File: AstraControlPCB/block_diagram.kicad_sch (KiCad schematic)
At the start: 0 parts

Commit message: Update wks file
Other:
- sheet 5V Protection: file 5V_Protection.kicad_sch -> 5v_protection.kicad_sch
- company: (none) -> LiveAstra Technologies
- title: Block Diagram -> AstraControl - Root
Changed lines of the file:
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@@
 	(paper "A4")
 	(title_block
-		(title "Block Diagram")
+		(title "AstraControl - Root")
+		(date "2024-08-26")
+		(rev "A")
+		(company "LiveAstra Technologies")
 	)
 	(junction
@@
 		(effects
 			(font
+				(face "ING Me")
 				(size 1.27 1.27)
 			)
@@
 		(effects
 			(font
+				(face "ING Me")
 				(size 1.27 1.27)
 			)
@@
 		(effects
 			(font
+				(face "ING Me")
 				(size 1.27 1.27)
 			)
@@
 		(effects
 			(font
+				(face "ING Me")
 				(size 1.27 1.27)
 			)
@@
 		(effects
 			(font
+				(face "ING Me")
 				(size 1.27 1.27)
 			)
@@
 		(effects
 			(font
+				(face "ING Me")
 				(size 1.27 1.27)
 			)
@@
 		(effects
 			(font
+				(face "ING Me")
 				(size 1.27 1.27)
 			)
@@
 		(effects
 			(font
+				(face "ING Me")
 				(size 1.27 1.27)
 			)
@@
 		(effects
 			(font
+				(face "ING Me")
 				(size 1.27 1.27)
 			)
@@
 		(effects
 			(font
+				(face "ING Me")
 				(size 1.27 1.27)
 			)
@@
 			)
 		)
-		(property "Sheetfile" "5V_Protection.kicad_sch"
+		(property "Sheetfile" "5v_protection.kicad_sch"
 			(at 50.8 33.6046 0)
 			(effects

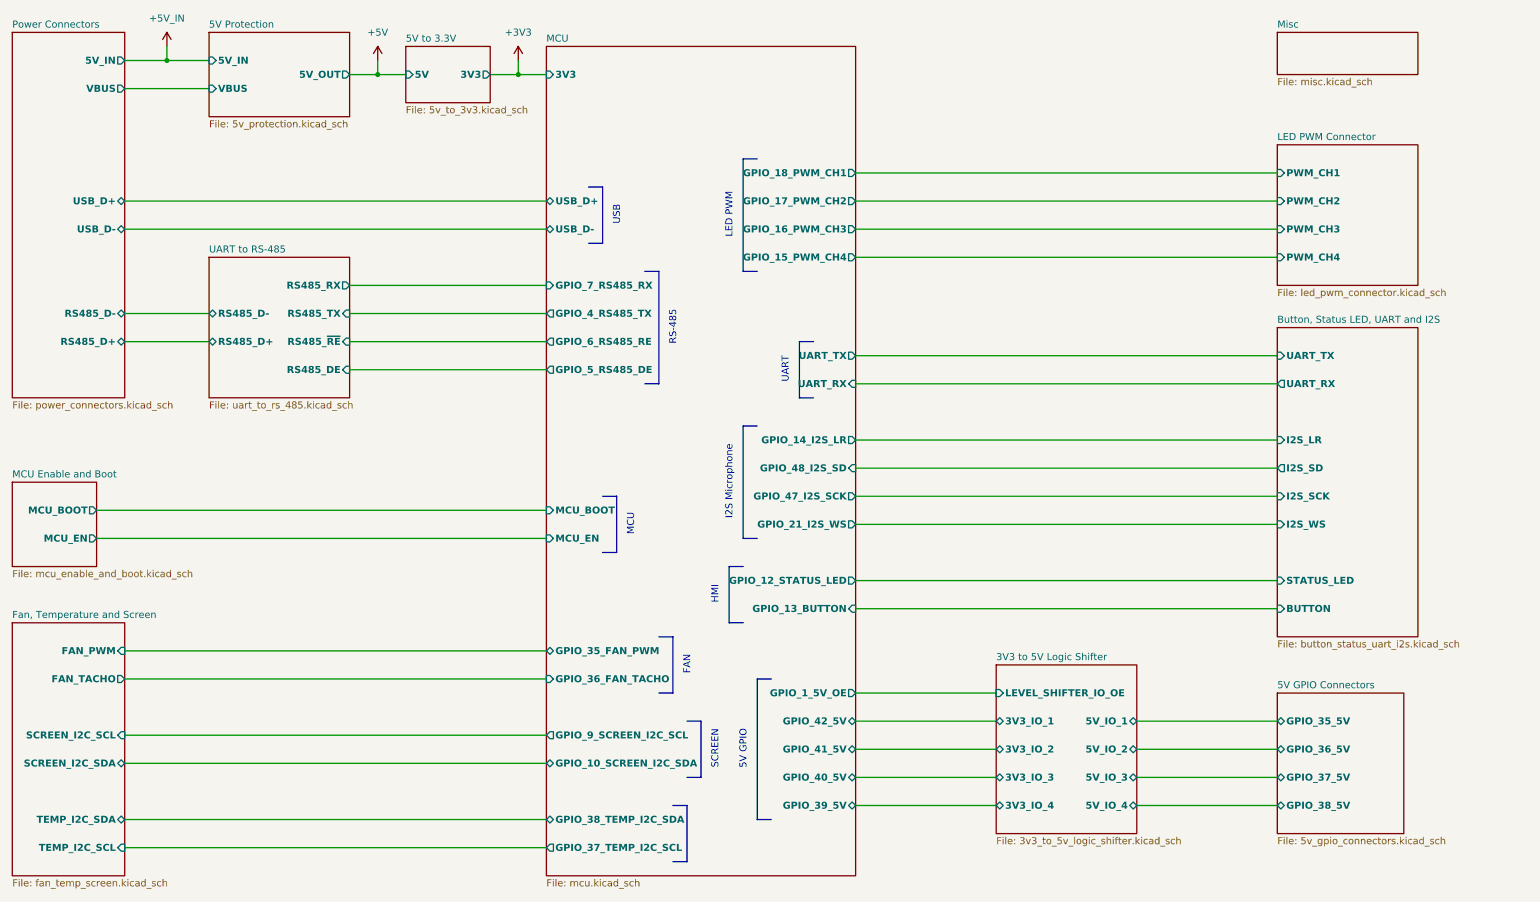
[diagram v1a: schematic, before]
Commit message: move template to root
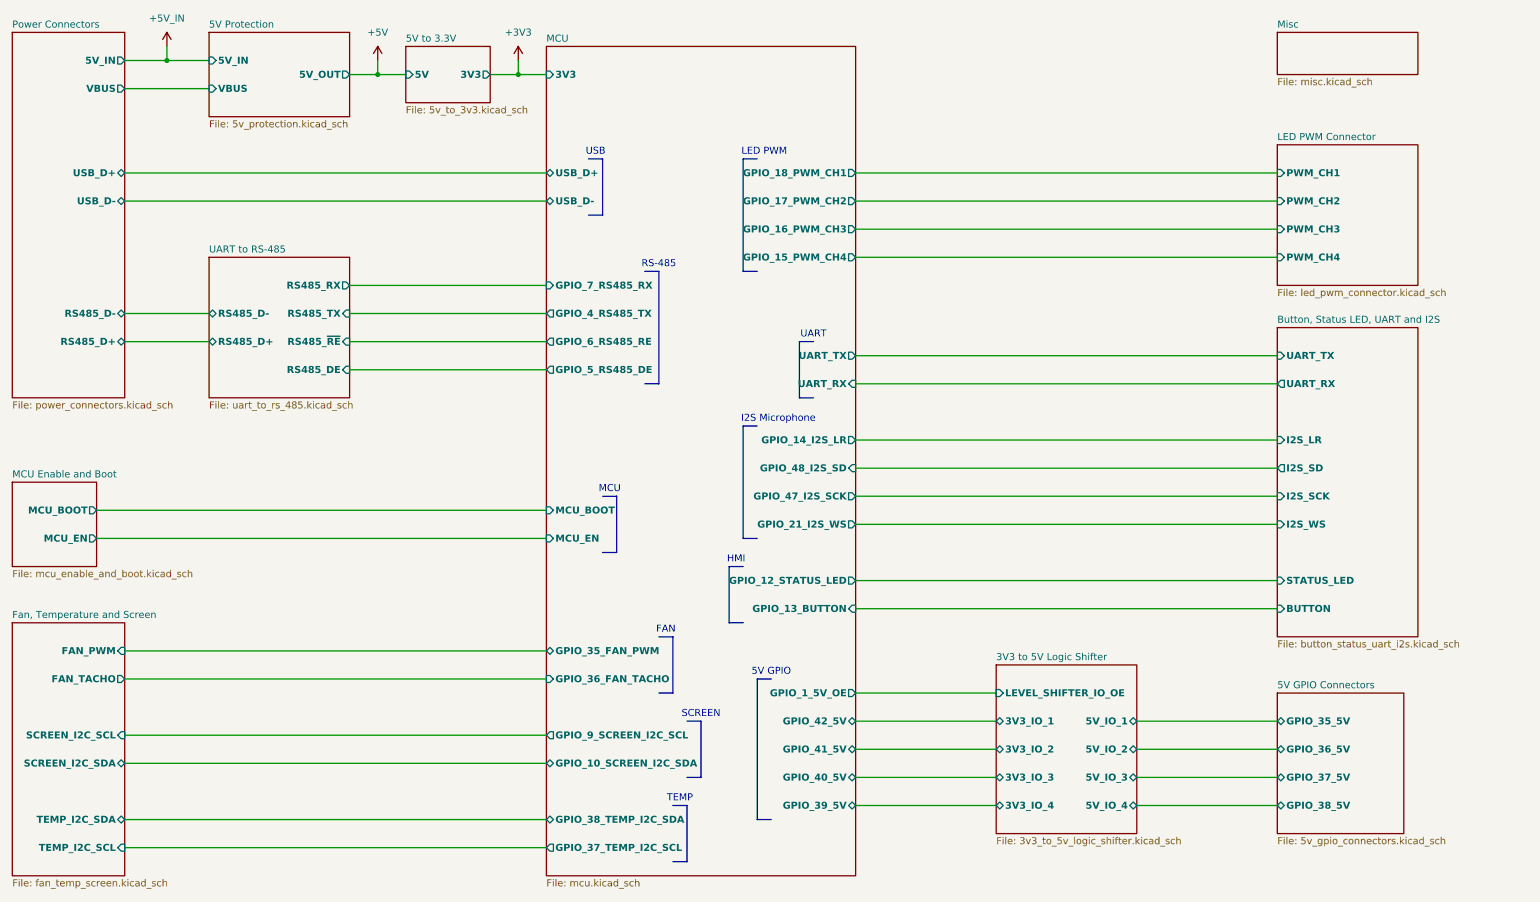
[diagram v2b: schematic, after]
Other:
- note added: "TEMP"
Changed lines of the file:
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@@
-	(wire
-		(pts
-			(xy 35.56 53.34) (xy 111.76 53.34)
-		)
-		(stroke
-			(width 0)
-			(type default)
-		)
-	)
 	(wire
 		(pts
@@
 		)
 	)
+	(polyline
+		(pts
+			(xy 121.92 40.64) (xy 121.92 50.8)
+		)
+		(stroke
+			(width 0)
+			(type default)
+		)
+	)
+	(wire
+		(pts
+			(xy 167.64 58.42) (xy 243.84 58.42)
+		)
+		(stroke
+			(width 0)
+			(type default)
+		)
+	)
+	(polyline
+		(pts
+			(xy 147.32 40.64) (xy 149.86 40.64)
+		)
+		(stroke
+			(width 0)
+			(type default)
+		)
+	)
+	(polyline
+		(pts
+			(xy 144.78 124.46) (xy 147.32 124.46)
+		)
+		(stroke
+			(width 0)
+			(type default)
+		)
+	)
+	(wire
+		(pts
+			(xy 35.56 165.1) (xy 111.76 165.1)
+		)
+		(stroke
+			(width 0)
+			(type default)
+		)
+	)
+	(wire
+		(pts
+			(xy 76.2 68.58) (xy 111.76 68.58)
+		)
+		(stroke
+			(width 0)
+			(type default)
+		)
+	)
+	(polyline
+		(pts
+			(xy 132.08 60.96) (xy 132.08 81.28)
+		)
+		(stroke
+			(width 0)
+			(type default)
+		)
+	)
+	(wire
+		(pts
+			(xy 167.64 53.34) (xy 243.84 53.34)
+		)
+		(stroke
+			(width 0)
+			(type default)
+		)
+	)
+	(wire
+		(pts
+			(xy 167.64 48.26) (xy 243.84 48.26)
+		)
+		(stroke
+			(width 0)
+			(type default)
+		)
+	)
+	(wire
+		(pts
+			(xy 167.64 81.28) (xy 243.84 81.28)
+		)
+		(stroke
+			(width 0)
+			(type default)
+		)
+	)
+	(wire
+		(pts
+			(xy 76.2 63.5) (xy 111.76 63.5)
+		)
+		(stroke
+			(width 0)
+			(type default)
+		)
+	)
+	(polyline
+		(pts
+			(xy 137.16 157.48) (xy 137.16 167.64)
+		)
+		(stroke
+			(width 0)
+			(type default)
+		)
+	)
 	(wire
 		(pts
@@
 	(polyline
 		(pts
-			(xy 121.92 45.72) (xy 121.92 55.88)
-		)
-		(stroke
-			(width 0)
-			(type default)
-		)
-	)
-	(wire
-		(pts
-			(xy 167.64 58.42) (xy 243.84 58.42)
-		)
-		(stroke
-			(width 0)
-			(type default)
-		)
-	)
-	(polyline
-		(pts
-			(xy 147.32 40.64) (xy 149.86 40.64)
-		)
-		(stroke
-			(width 0)
-			(type default)
-		)
-	)
-	(polyline
-		(pts
-			(xy 144.78 124.46) (xy 147.32 124.46)
-		)
-		(stroke
-			(width 0)
-			(type default)
-		)
-	)
-	(wire
-		(pts
-			(xy 35.56 165.1) (xy 111.76 165.1)
-		)
-		(stroke
-			(width 0)
-			(type default)
-		)
-	)
-	(wire
-		(pts
-			(xy 76.2 68.58) (xy 111.76 68.58)
-		)
-		(stroke
-			(width 0)
-			(type default)
-		)
-	)
-	(polyline
-		(pts
-			(xy 132.08 60.96) (xy 132.08 81.28)
-		)
-		(stroke
-			(width 0)
-			(type default)
-		)
-	)
-	(wire
-		(pts
-			(xy 167.64 53.34) (xy 243.84 53.34)
-		)
-		(stroke
-			(width 0)
-			(type default)
-		)
-	)
-	(wire
-		(pts
-			(xy 167.64 48.26) (xy 243.84 48.26)
-		)
-		(stroke
-			(width 0)
-			(type default)
-		)
-	)
-	(wire
-		(pts
-			(xy 167.64 81.28) (xy 243.84 81.28)
-		)
-		(stroke
-			(width 0)
-			(type default)
-		)
-	)
-	(wire
-		(pts
-			(xy 76.2 63.5) (xy 111.76 63.5)
-		)
-		(stroke
-			(width 0)
-			(type default)
-		)
-	)
-	(polyline
-		(pts
-			(xy 137.16 157.48) (xy 137.16 167.64)
-		)
-		(stroke
-			(width 0)
-			(type default)
-		)
-	)
-	(polyline
-		(pts
 			(xy 121.92 101.6) (xy 124.46 101.6)
 		)
@@
 	(polyline
 		(pts
-			(xy 119.38 45.72) (xy 121.92 45.72)
+			(xy 119.38 40.64) (xy 121.92 40.64)
 		)
 		(stroke
@@
 	(polyline
 		(pts
-			(xy 119.38 55.88) (xy 121.92 55.88)
+			(xy 119.38 50.8) (xy 121.92 50.8)
 		)
 		(stroke
@@
 		(pts
 			(xy 35.56 68.58) (xy 50.8 68.58)
+		)
+		(stroke
+			(width 0)
+			(type default)
+		)
+	)
+	(wire
+		(pts
+			(xy 35.56 43.18) (xy 111.76 43.18)
 		)
 		(stroke
@@
 	(text "USB"
 		(exclude_from_sim no)
-		(at 124.46 50.8 90)
+		(at 120.65 39.37 0)
 		(effects
 			(font
@@
 	(text "FAN"
 		(exclude_from_sim no)
-		(at 137.16 132.08 90)
+		(at 133.35 125.73 0)
 		(effects
 			(font
@@
 	(text "LED PWM"
 		(exclude_from_sim no)
-		(at 144.78 50.8 90)
+		(at 151.13 39.37 0)
 		(effects
 			(font
@@
 	(text "MCU"
 		(exclude_from_sim no)
-		(at 127 106.68 90)
+		(at 123.19 100.33 0)
 		(effects
 			(font
@@
 	(text "I2S Microphone"
 		(exclude_from_sim no)
-		(at 144.78 99.06 90)
+		(at 153.67 87.63 0)
 		(effects
 			(font
@@
 	(text "5V GPIO"
 		(exclude_from_sim no)
-		(at 147.32 147.32 90)
+		(at 152.4 133.35 0)
 		(effects
 			(font
@@
 	(text "RS-485"
 		(exclude_from_sim no)
-		(at 134.62 71.12 90)
+		(at 132.08 59.69 0)
 		(effects
 			(font
@@
 	(text "UART"
 		(exclude_from_sim no)
-		(at 154.94 78.74 90)
+		(at 160.02 72.39 0)
 		(effects
 			(font
@@
 	(text "SCREEN"
 		(exclude_from_sim no)
-		(at 142.24 147.32 90)
+		(at 139.7 140.97 0)
 		(effects
 			(font
@@
 	(text "HMI"
 		(exclude_from_sim no)
-		(at 142.24 119.38 90)
+		(at 146.05 113.03 0)
+		(effects
+			(font
+				(face "ING Me")
+				(size 1.27 1.27)
+			)
+		)
+	)
+	(text "TEMP"
+		(exclude_from_sim no)
+		(at 135.89 156.21 0)
 		(effects
 			(font
@@
 		)
 		(pin "USB_D-" bidirectional
-			(at 111.76 53.34 180)
+			(at 111.76 48.26 180)
 			(effects
 				(font
@@
 		)
 		(pin "USB_D+" bidirectional
-			(at 111.76 48.26 180)
+			(at 111.76 43.18 180)
 			(effects
 				(font
@@
 		)
 		(pin "USB_D-" bidirectional
-			(at 35.56 53.34 0)
+			(at 35.56 48.26 0)
 			(effects
 				(font
@@
 		)
 		(pin "USB_D+" bidirectional
-			(at 35.56 48.26 0)
-			(effects
-				(font
+			(at 35.56 43.18 0)
+			(effects
+				(font
